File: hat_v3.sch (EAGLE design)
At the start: 25 parts, among them U1 ADS1115IDGST, U2 ADXL345

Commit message: V3 almost done, just need to finish MCP2515
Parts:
- added C7, C8: 560pF, microbuilder:CAP_CERAMIC0805
- added C9: 0.1µF, microbuilder:CAP_CERAMIC0805
- added FRAME2: FRAME-LETTERNO_PACKAGE, SparkFun-Aesthetics:FRAME-LETTERNO_PACKAGE
- added J3: (no value), SparkFun-Connectors:M025MM
- added R10, R11: 100, SparkFun-Passives:RESISTOR0805-RES
- added R12: 10k, SparkFun-Passives:RESISTOR0805-RES
- added R13: 22k, SparkFun-Passives:RESISTOR0805-RES
- added R9: 4k7, SparkFun-Passives:RESISTOR0805-RES
- added U5: MCP2515-I/ST, mcp2515:MCP2515-I/ST
- added U6: MCP2551, SparkFun-DigitalIC:MCP2551
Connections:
- removed net 5.0V: RPI1.5.0V, RPI1.5.0V@1
- new net 5V: C9.P$1, RPI1.5.0V, RPI1.5.0V@1, U6.VSS
- new net CANH: J3.1, R10.2, U6.CANH
- new net CANL: J3.2, R11.2, U6.CANL
- new net N$4: R12.1, R13.2, U5.RXCAN
- new net N$5: R9.2, U6.RS
- new net N$6: C7.P$1, R10.1
- new net N$8: C8.P$1, R11.1
- new net RXCAN: R12.2, U6.RXD
- new net TXCAN: U5.TXCAN, U6.TXD
- net GND: now also C7.P$2, C8.P$2, C9.P$2, R13.1, R9.1, U6.VDD
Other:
- note added: "v3"
- note removed: "v1"

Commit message: V3 done!
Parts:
- added C10: 100nF, microbuilder:CAP_CERAMIC0805
- added C11, C12: 22pF, microbuilder:CAP_CERAMIC0805
- added R14: 4k7, SparkFun-Passives:RESISTOR0805-RES
- added X1: 16Mhz, IQD-Frequency-Products:CRYSTALS-NOGND-4-HSMX
- U5: value MCP2515-I/ST -> MCP2515-I/SO; device mcp2515:MCP2515-I/ST -> mcp2515:MCP2515-I/SO
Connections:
- new net N$14: C12.P$1, U5.OSC1, X1.2
- new net N$15: C11.P$1, U5.OSC2, X1.1
- new net U5_RST: R14.1, U5.RESET
- net 3.3V: now also C10.P$1, R14.2, U5.VDD
- net GND: now also C10.P$2, C11.P$2, C12.P$2, U5.VSS
- net GPIO25: now also U5.INT
- net SPI_CE0: now also U5.CS
- net SPI_MISO: now also U5.SO
- net SPI_MOSI: now also U5.SI
- net SPI_SCLK: now also U5.SCK
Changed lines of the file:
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@@
 <part name="D1" library="diode" deviceset="DIODE-" device="DO214AC"/>
 <part name="SUPPLY9" library="SparkFun-Aesthetics" deviceset="5V" device=""/>
-<part name="U5" library="mcp2515" deviceset="MCP2515" device="-I/ST"/>
 <part name="U6" library="SparkFun-DigitalIC" deviceset="MCP2551" device=""/>
 <part name="R9" library="SparkFun-Passives" deviceset="RESISTOR" device="0805-RES" value="4k7"/>
@@
 <part name="R13" library="SparkFun-Passives" deviceset="RESISTOR" device="0805-RES" value="22k"/>
 <part name="GND6" library="SparkFun-Aesthetics" deviceset="GND" device=""/>
+<part name="SUPPLY10" library="SparkFun-Aesthetics" deviceset="3.3V" device=""/>
+<part name="R14" library="SparkFun-Passives" deviceset="RESISTOR" device="0805-RES" value="4k7"/>
+<part name="SUPPLY12" library="SparkFun-Aesthetics" deviceset="3.3V" device=""/>
+<part name="C10" library="microbuilder" deviceset="CAP_CERAMIC" device="0805" value="100nF"/>
+<part name="GND8" library="SparkFun-Aesthetics" deviceset="GND" device=""/>
+<part name="GND9" library="SparkFun-Aesthetics" deviceset="GND" device=""/>
+<part name="X1" library="IQD-Frequency-Products" deviceset="CRYSTALS-NOGND" device="-4-HSMX" value="16Mhz"/>
+<part name="C11" library="microbuilder" deviceset="CAP_CERAMIC" device="0805" value="22pF"/>
+<part name="C12" library="microbuilder" deviceset="CAP_CERAMIC" device="0805" value="22pF"/>
+<part name="GND10" library="SparkFun-Aesthetics" deviceset="GND" device=""/>
+<part name="U5" library="mcp2515" deviceset="MCP2515" device="-I/SO"/>
 </parts>
 <sheets>
@@
 </plain>
 <instances>
-<instance part="U5" gate="G$1" x="58.42" y="99.06"/>
 <instance part="U6" gate="MCP2551" x="53.34" y="38.1"/>
 <instance part="R9" gate="G$1" x="83.82" y="27.94" rot="R90"/>
@@
 <instance part="R12" gate="G$1" x="116.84" y="106.68"/>
 <instance part="R13" gate="G$1" x="106.68" y="96.52" rot="R90"/>
-<instance part="GND6" gate="1" x="106.68" y="86.36"/>
+<instance part="GND6" gate="1" x="106.68" y="78.74"/>
+<instance part="SUPPLY10" gate="G$1" x="35.56" y="129.54"/>
+<instance part="R14" gate="G$1" x="35.56" y="121.92" rot="R90"/>
+<instance part="SUPPLY12" gate="G$1" x="83.82" y="134.62"/>
+<instance part="C10" gate="G$1" x="83.82" y="124.46"/>
+<instance part="GND8" gate="1" x="83.82" y="116.84"/>
+<instance part="GND9" gate="1" x="76.2" y="78.74"/>
+<instance part="X1" gate="G$1" x="78.74" y="93.98" rot="R90"/>
+<instance part="C11" gate="G$1" x="88.9" y="88.9" rot="R90"/>
+<instance part="C12" gate="G$1" x="88.9" y="99.06" rot="R90"/>
+<instance part="GND10" gate="1" x="93.98" y="78.74"/>
+<instance part="U5" gate="G$1" x="58.42" y="99.06"/>
 </instances>
 <busses>
@@
 <pinref part="R13" gate="G$1" pin="1"/>
 <pinref part="GND6" gate="1" pin="GND"/>
-<wire x1="106.68" y1="91.44" x2="106.68" y2="88.9" width="0.1524" layer="91"/>
+<wire x1="106.68" y1="91.44" x2="106.68" y2="81.28" width="0.1524" layer="91"/>
+</segment>
+<segment>
+<pinref part="GND8" gate="1" pin="GND"/>
+<pinref part="C10" gate="G$1" pin="P$2"/>
+<wire x1="83.82" y1="119.38" x2="83.82" y2="121.92" width="0.1524" layer="91"/>
+</segment>
+<segment>
+<pinref part="GND9" gate="1" pin="GND"/>
+<wire x1="73.66" y1="83.82" x2="76.2" y2="83.82" width="0.1524" layer="91"/>
+<wire x1="76.2" y1="83.82" x2="76.2" y2="81.28" width="0.1524" layer="91"/>
+<pinref part="U5" gate="G$1" pin="VSS"/>
+</segment>
+<segment>
+<pinref part="C11" gate="G$1" pin="P$2"/>
+<wire x1="91.44" y1="88.9" x2="93.98" y2="88.9" width="0.1524" layer="91"/>
+<wire x1="93.98" y1="88.9" x2="93.98" y2="81.28" width="0.1524" layer="91"/>
+<pinref part="C12" gate="G$1" pin="P$2"/>
+<wire x1="91.44" y1="99.06" x2="93.98" y2="99.06" width="0.1524" layer="91"/>
+<wire x1="93.98" y1="99.06" x2="93.98" y2="88.9" width="0.1524" layer="91"/>
+<pinref part="GND10" gate="1" pin="GND"/>
+<junction x="93.98" y="88.9"/>
 </segment>
 </net>
@@
 </segment>
 <segment>
-<pinref part="U5" gate="G$1" pin="TXCAN"/>
 <wire x1="73.66" y1="109.22" x2="83.82" y2="109.22" width="0.1524" layer="91"/>
 <label x="76.2" y="109.22" size="1.778" layer="95"/>
+<pinref part="U5" gate="G$1" pin="TXCAN"/>
 </segment>
 </net>
@@
 <segment>
 <pinref part="R12" gate="G$1" pin="1"/>
-<pinref part="U5" gate="G$1" pin="RXCAN"/>
 <wire x1="111.76" y1="106.68" x2="106.68" y2="106.68" width="0.1524" layer="91"/>
 <pinref part="R13" gate="G$1" pin="2"/>
@@
 <wire x1="106.68" y1="101.6" x2="106.68" y2="106.68" width="0.1524" layer="91"/>
 <junction x="106.68" y="106.68"/>
+<pinref part="U5" gate="G$1" pin="RXCAN"/>
+</segment>
+</net>
+<net name="3.3V" class="0">
+<segment>
+<wire x1="35.56" y1="127" x2="35.56" y2="129.54" width="0.1524" layer="91"/>
+<pinref part="SUPPLY10" gate="G$1" pin="3.3V"/>
+<pinref part="R14" gate="G$1" pin="2"/>
+</segment>
+<segment>
+<pinref part="C10" gate="G$1" pin="P$1"/>
+<pinref part="SUPPLY12" gate="G$1" pin="3.3V"/>
+<wire x1="83.82" y1="129.54" x2="83.82" y2="132.08" width="0.1524" layer="91"/>
+<wire x1="83.82" y1="132.08" x2="83.82" y2="134.62" width="0.1524" layer="91"/>
+<wire x1="73.66" y1="114.3" x2="78.74" y2="114.3" width="0.1524" layer="91"/>
+<wire x1="78.74" y1="114.3" x2="78.74" y2="132.08" width="0.1524" layer="91"/>
+<wire x1="78.74" y1="132.08" x2="83.82" y2="132.08" width="0.1524" layer="91"/>
+<junction x="83.82" y="132.08"/>
+<pinref part="U5" gate="G$1" pin="VDD"/>
+</segment>
+</net>
+<net name="U5_RST" class="0">
+<segment>
+<wire x1="43.18" y1="114.3" x2="35.56" y2="114.3" width="0.1524" layer="91"/>
+<wire x1="35.56" y1="114.3" x2="35.56" y2="116.84" width="0.1524" layer="91"/>
+<pinref part="R14" gate="G$1" pin="1"/>
+<pinref part="U5" gate="G$1" pin="RESET"/>
+</segment>
+</net>
+<net name="SPI_CE0" class="0">
+<segment>
+<wire x1="43.18" y1="111.76" x2="30.48" y2="111.76" width="0.1524" layer="91"/>
+<label x="30.48" y="111.76" size="1.778" layer="95"/>
+<pinref part="U5" gate="G$1" pin="CS"/>
+</segment>
+</net>
+<net name="SPI_SCLK" class="0">
+<segment>
+<wire x1="43.18" y1="104.14" x2="30.48" y2="104.14" width="0.1524" layer="91"/>
+<label x="30.48" y="104.14" size="1.778" layer="95"/>
+<pinref part="U5" gate="G$1" pin="SCK"/>
+</segment>
+</net>
+<net name="GPIO25" class="0">
+<segment>
+<wire x1="43.18" y1="99.06" x2="30.48" y2="99.06" width="0.1524" layer="91"/>
+<label x="30.48" y="99.06" size="1.778" layer="95"/>
+<pinref part="U5" gate="G$1" pin="INT"/>
+</segment>
+</net>
+<net name="N$14" class="0">
+<segment>
+<wire x1="73.66" y1="99.06" x2="78.74" y2="99.06" width="0.1524" layer="91"/>
+<pinref part="X1" gate="G$1" pin="2"/>
+<wire x1="78.74" y1="99.06" x2="78.74" y2="96.52" width="0.1524" layer="91"/>
+<pinref part="C12" gate="G$1" pin="P$1"/>
+<wire x1="78.74" y1="99.06" x2="83.82" y2="99.06" width="0.1524" layer="91"/>
+<junction x="78.74" y="99.06"/>
+<pinref part="U5" gate="G$1" pin="OSC1"/>
+</segment>
+</net>
+<net name="N$15" class="0">
+<segment>
+<wire x1="73.66" y1="88.9" x2="78.74" y2="88.9" width="0.1524" layer="91"/>
+<pinref part="X1" gate="G$1" pin="1"/>
+<wire x1="78.74" y1="88.9" x2="78.74" y2="91.44" width="0.1524" layer="91"/>
+<pinref part="C11" gate="G$1" pin="P$1"/>
+<wire x1="83.82" y1="88.9" x2="78.74" y2="88.9" width="0.1524" layer="91"/>
+<junction x="78.74" y="88.9"/>
+<pinref part="U5" gate="G$1" pin="OSC2"/>
+</segment>
+</net>
+<net name="SPI_MISO" class="0">
+<segment>
+<wire x1="43.18" y1="109.22" x2="30.48" y2="109.22" width="0.1524" layer="91"/>
+<label x="30.48" y="109.22" size="1.778" layer="95"/>
+<pinref part="U5" gate="G$1" pin="SO"/>
+</segment>
+</net>
+<net name="SPI_MOSI" class="0">
+<segment>
+<wire x1="43.18" y1="106.68" x2="30.48" y2="106.68" width="0.1524" layer="91"/>
+<label x="30.48" y="106.68" size="1.778" layer="95"/>
+<pinref part="U5" gate="G$1" pin="SI"/>
 </segment>
 </net>
@@
 </sheet>
 </sheets>
+<errors>
+</errors>
 </schematic>
 </drawing>

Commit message: Reworked v3
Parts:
- removed R13: 22k, SparkFun-Passives:RESISTOR0805-RES
- removed R14: 4k7, SparkFun-Passives:RESISTOR0805-RES
- added D2: (no value), diode:DIODE-2CA|ACSOT23
- C1, C2: value 100uF -> 10uF; device SparkFun:CAP_POL1206 -> SparkFun-Capacitors:CAP_POL1206
- C10: value 100nF -> 0.1uF
- C6: device SparkFun:CAP_POL1206 -> SparkFun-Capacitors:CAP_POL1206
- R10: value 100 -> 10k
- R11: value 100 -> 22k
- R12, R7: value 10k -> 4k7
- R8: value 10k -> 100
- R9: value 4k7 -> 100
- renumbered U5 to U3, U6 to U4
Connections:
- net 3.3V: now also R12.2; no longer R14.2, R6.2, R7.2
- net ADDR: now also R6.2; no longer R8.2
- net BAT-1-INPUT: now also D2.K1; no longer VD1.C
- net BAT-2-INPUT: now also D2.K2; no longer VD2.C
- net CANH: now also R8.2; no longer R10.2
- net CANL: now also R9.2; no longer R11.2
- net GND: now also D2.A, R11.1, R6.1, R7.1; no longer R13.1, R8.1, R9.1
- net N$4: now also R10.1, R11.2; no longer R12.1, R13.2
- net N$5: now also R7.2; no longer R9.2
- net N$6: now also R8.1; no longer R10.1
- net N$8: now also R9.1; no longer R11.1
- net RXCAN: now also R10.2; no longer R12.2
- net SCL: no longer R6.1
- net SDA: no longer R7.1
- net SHUNT-HIGH-INPUT: now also VD1.C
- net SHUNT-LOW-INPUT: now also VD2.C
- net U5_RST: now also R12.1; no longer R14.1
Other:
- moved on the sheet: OK1, R10, R11, R12, R5, R6, R9, VD1, VD2

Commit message: Minor tweaks to GND plane
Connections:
- net N$1 renamed VEHICLE-GND
- net N$5 renamed RS
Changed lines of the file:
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@@
 </segment>
 </net>
-<net name="N$1" class="0">
+<net name="VEHICLE-GND" class="0">
 <segment>
 <pinref part="J1" gate="J$1" pin="1"/>
@@
 </segment>
 </net>
-<net name="N$5" class="0">
+<net name="RS" class="0">
 <segment>
 <pinref part="U4" gate="MCP2551" pin="RS"/>

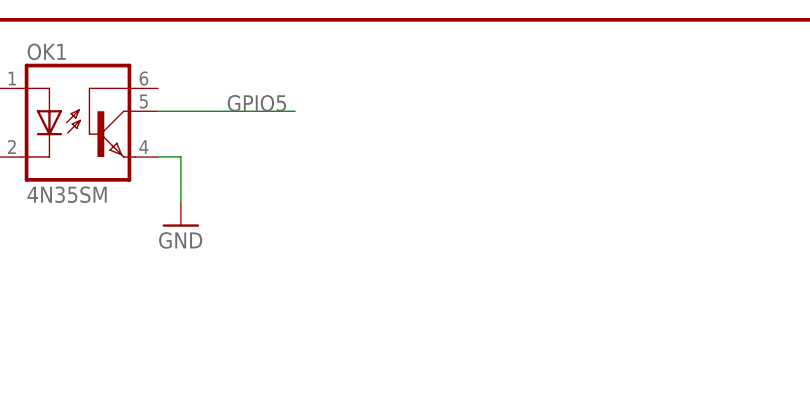
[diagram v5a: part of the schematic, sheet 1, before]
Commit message: Switched to 3.5mm screw terminals
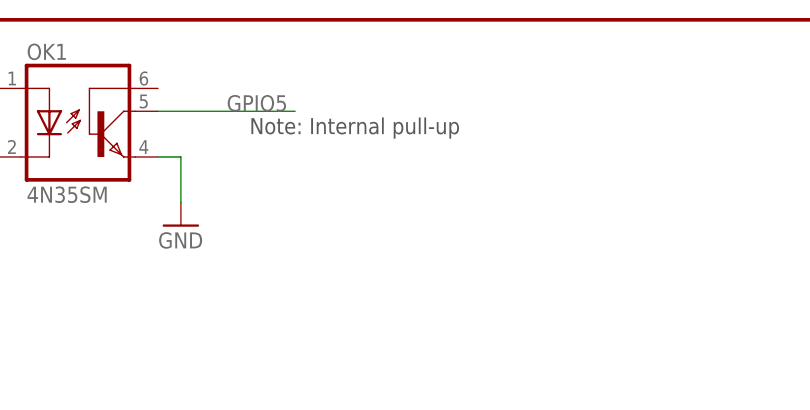
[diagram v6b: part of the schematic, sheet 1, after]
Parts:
- J1, J2: device SparkFun-Connectors:M03-SCREW-5MM -> SparkFun-Connectors:M03SCREW
- J3: device SparkFun-Connectors:M025MM -> SparkFun-Connectors:M023.5MM
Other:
- note added: "Note: Internal pull-up"
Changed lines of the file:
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@@
 <part name="GND4" library="SparkFun-Aesthetics" deviceset="GND" device=""/>
 <part name="GPS" library="SparkFun-Connectors" deviceset="M05" device="PTH"/>
-<part name="J1" library="SparkFun-Connectors" deviceset="M03" device="-SCREW-5MM"/>
-<part name="J2" library="SparkFun-Connectors" deviceset="M03" device="-SCREW-5MM"/>
 <part name="GND5" library="SparkFun-Aesthetics" deviceset="GND" device=""/>
 <part name="GND7" library="SparkFun-Aesthetics" deviceset="GND" device=""/>
@@
 <part name="GND18" library="SparkFun-Aesthetics" deviceset="GND" device=""/>
 <part name="GND19" library="SparkFun-Aesthetics" deviceset="GND" device=""/>
-<part name="J3" library="SparkFun-Connectors" deviceset="M02" device="5MM"/>
 <part name="FRAME2" library="SparkFun-Aesthetics" deviceset="FRAME-LETTER" device="NO_PACKAGE"/>
 <part name="R10" library="SparkFun-Passives" deviceset="RESISTOR" device="0805-RES" value="10k"/>
@@
 <part name="GND20" library="SparkFun-Aesthetics" deviceset="GND" device=""/>
 <part name="GND21" library="SparkFun-Aesthetics" deviceset="GND" device=""/>
+<part name="J1" library="SparkFun-Connectors" deviceset="M03" device="SCREW"/>
+<part name="J2" library="SparkFun-Connectors" deviceset="M03" device="SCREW"/>
+<part name="J3" library="SparkFun-Connectors" deviceset="M02" device="3.5MM"/>
 </parts>
 <sheets>
@@
 <text x="241.3" y="7.62" size="2.54" layer="94">v3</text>
 <text x="106.68" y="17.78" size="1.778" layer="97">Default I²C Address = 1001000</text>
+<text x="101.6" y="172.72" size="1.778" layer="97">Note: Internal pull-up</text>
 </plain>
 <instances>
@@
 <instance part="GND4" gate="1" x="226.06" y="124.46"/>
 <instance part="GPS" gate="G$1" x="7.62" y="139.7"/>
-<instance part="J1" gate="J$1" x="7.62" y="160.02"/>
-<instance part="J2" gate="J$1" x="7.62" y="175.26"/>
 <instance part="GND5" gate="1" x="71.12" y="160.02"/>
 <instance part="GND7" gate="1" x="93.98" y="162.56"/>
@@
 <instance part="GND20" gate="1" x="50.8" y="160.02"/>
 <instance part="GND21" gate="1" x="43.18" y="160.02"/>
+<instance part="J1" gate="J$1" x="7.62" y="160.02"/>
+<instance part="J2" gate="J$1" x="7.62" y="175.26"/>
 </instances>
 <busses>
@@
 <net name="BAT-1-INPUT" class="0">
 <segment>
-<pinref part="J1" gate="J$1" pin="2"/>
 <wire x1="15.24" y1="160.02" x2="33.02" y2="160.02" width="0.1524" layer="91"/>
 <label x="17.78" y="160.02" size="1.778" layer="95"/>
+<pinref part="J1" gate="J$1" pin="2"/>
 </segment>
 <segment>
@@
 <net name="BAT-2-INPUT" class="0">
 <segment>
-<pinref part="J1" gate="J$1" pin="3"/>
 <wire x1="15.24" y1="162.56" x2="33.02" y2="162.56" width="0.1524" layer="91"/>
 <label x="17.78" y="162.56" size="1.778" layer="95"/>
+<pinref part="J1" gate="J$1" pin="3"/>
 </segment>
 <segment>
@@
 <net name="SHUNT-HIGH-INPUT" class="0">
 <segment>
-<pinref part="J2" gate="J$1" pin="1"/>
 <label x="17.78" y="172.72" size="1.778" layer="95"/>
 <pinref part="VD1" gate="G$1" pin="C"/>
 <wire x1="43.18" y1="170.18" x2="43.18" y2="172.72" width="0.1524" layer="91"/>
 <wire x1="43.18" y1="172.72" x2="15.24" y2="172.72" width="0.1524" layer="91"/>
+<pinref part="J2" gate="J$1" pin="1"/>
 </segment>
 <segment>
@@
 <net name="SHUNT-LOW-INPUT" class="0">
 <segment>
-<pinref part="J2" gate="J$1" pin="2"/>
 <label x="17.78" y="175.26" size="1.778" layer="95"/>
 <pinref part="VD2" gate="G$1" pin="C"/>
 <wire x1="50.8" y1="170.18" x2="50.8" y2="175.26" width="0.1524" layer="91"/>
 <wire x1="15.24" y1="175.26" x2="50.8" y2="175.26" width="0.1524" layer="91"/>
+<pinref part="J2" gate="J$1" pin="2"/>
 </segment>
 <segment>
@@
 <net name="LINKED-INPUT" class="0">
 <segment>
-<pinref part="J2" gate="J$1" pin="3"/>
 <wire x1="15.24" y1="177.8" x2="58.42" y2="177.8" width="0.1524" layer="91"/>
 <label x="17.78" y="177.8" size="1.778" layer="95"/>
 <pinref part="R5" gate="G$1" pin="1"/>
+<pinref part="J2" gate="J$1" pin="3"/>
 </segment>
 </net>
@@
 <net name="VEHICLE-GND" class="0">
 <segment>
-<pinref part="J1" gate="J$1" pin="1"/>
 <wire x1="17.78" y1="157.48" x2="15.24" y2="157.48" width="0.1524" layer="91"/>
 <pinref part="D1" gate="G$1" pin="C"/>
+<pinref part="J1" gate="J$1" pin="1"/>
 </segment>
 </net>
@@
 <instance part="GND18" gate="1" x="22.86" y="27.94"/>
 <instance part="GND19" gate="1" x="33.02" y="27.94"/>
-<instance part="J3" gate="G$1" x="127" y="43.18" rot="R180"/>
 <instance part="FRAME2" gate="G$1" x="0" y="0"/>
 <instance part="FRAME2" gate="V" x="147.32" y="0"/>
@@
 <instance part="GND10" gate="1" x="93.98" y="78.74"/>
 <instance part="U3" gate="G$1" x="58.42" y="99.06"/>
+<instance part="J3" gate="G$1" x="127" y="43.18" rot="R180"/>
 </instances>
 <busses>
